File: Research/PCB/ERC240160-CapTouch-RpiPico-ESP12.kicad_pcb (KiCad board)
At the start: 2 copper layers, 96.5 x 71.1 mm, 16 parts, among them U1 Pico, U2 ESP-12F

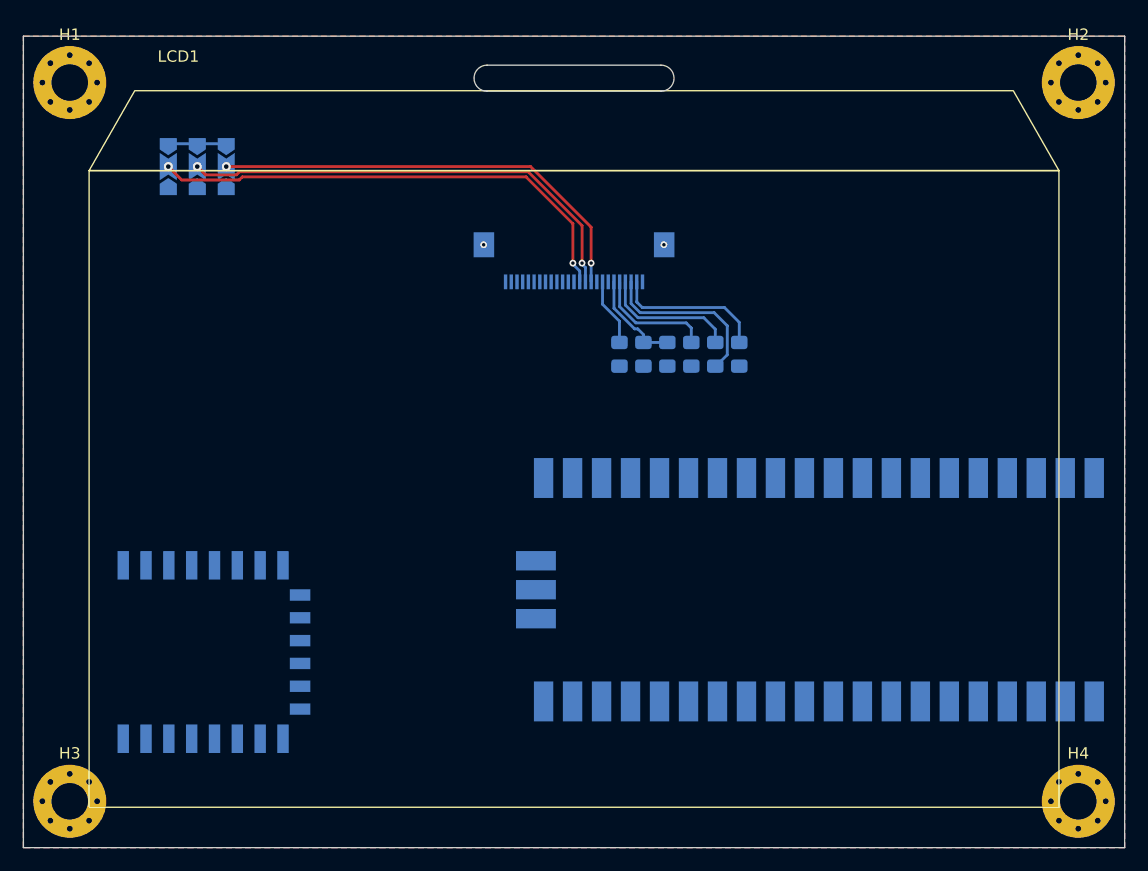
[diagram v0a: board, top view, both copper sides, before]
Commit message: Add 3D model for the Pico
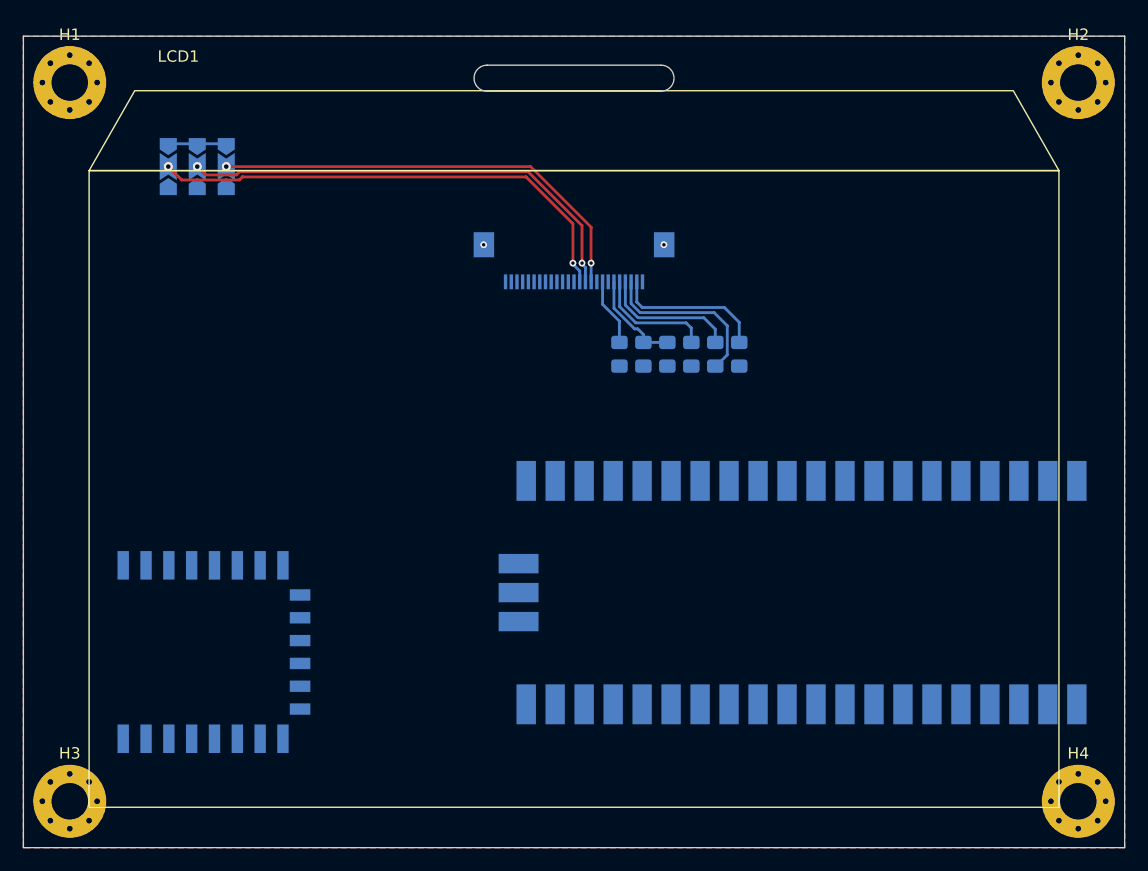
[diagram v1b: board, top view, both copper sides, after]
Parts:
- moved U1 1.55 mm to (167.3, 107.2)
